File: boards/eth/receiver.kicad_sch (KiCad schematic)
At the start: 10 parts, among them U16 74HC74, U17 74HC04, U18 74HC161, U19 74HC4040, U20 74HC164, U7 74HC08

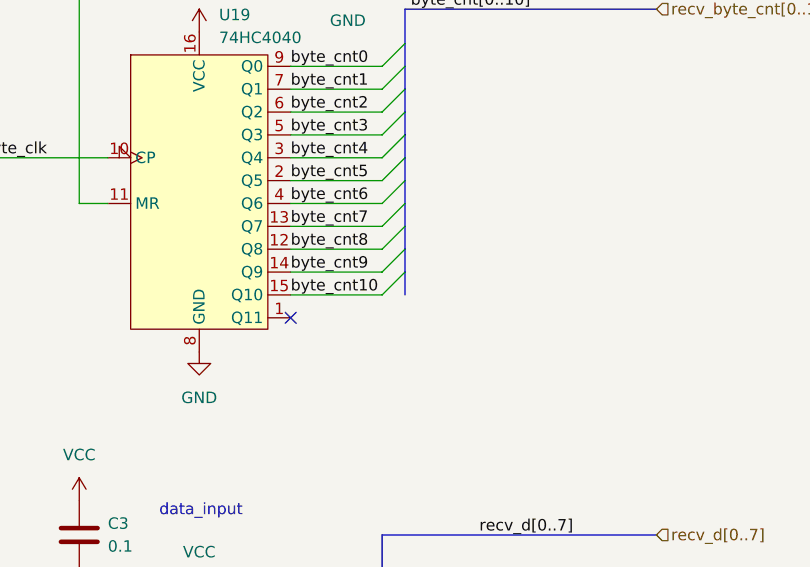
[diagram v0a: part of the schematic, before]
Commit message: Eth: transmitter schematics finished
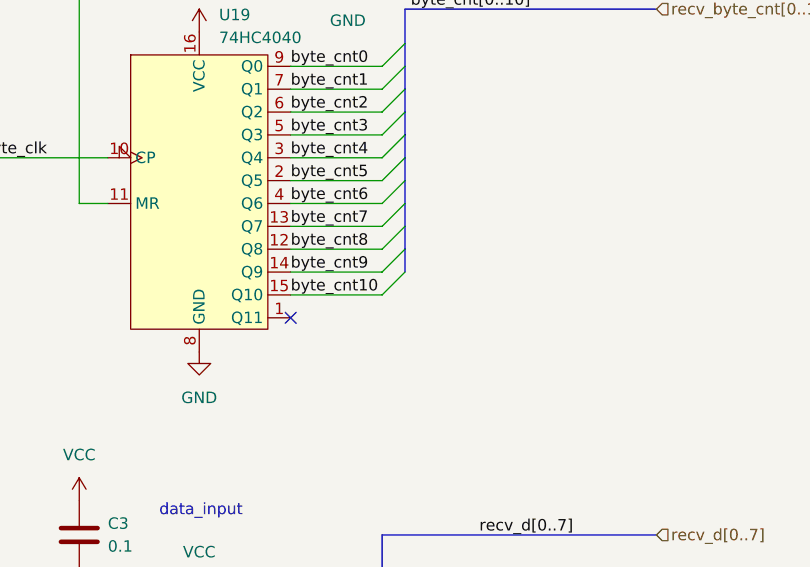
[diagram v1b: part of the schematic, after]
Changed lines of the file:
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@@
-    (stroke (width 0) (type default))
-  )
-  (bus (pts (xy 189.23 62.865) (xy 189.23 60.325))
     (stroke (width 0) (type default))
   )

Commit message: Eth: schematics checked
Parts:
- C30: renamed from C1; footprint (none) -> Capacitor_SMD:C_0805_2012Metric
- C31: renamed from C2; footprint (none) -> Capacitor_SMD:C_0805_2012Metric
- C32: renamed from C3; footprint (none) -> Capacitor_SMD:C_0805_2012Metric
- C33: renamed from C4; footprint (none) -> Capacitor_SMD:C_0805_2012Metric
- U29: renamed from U16; footprint (none) -> Package_SO:TSSOP-14_4.4x5mm_P0.65mm
- U30: renamed from U18; footprint (none) -> Package_SO:TSSOP-16_4.4x5mm_P0.65mm
- U31: renamed from U19; footprint (none) -> Package_SO:TSSOP-16_4.4x5mm_P0.65mm
- U32: renamed from U20; footprint (none) -> Package_SO:TSSOP-14_4.4x5mm_P0.65mm
- U6: renamed from U7; footprint (none) -> Package_SO:TSSOP-14_4.4x5mm_P0.65mm
- U9: renamed from U17; footprint (none) -> Package_SO:TSSOP-14_4.4x5mm_P0.65mm

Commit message: Eth: untangle schematic
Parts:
- removed U9: 74HC04, Package_SO:TSSOP-14_4.4x5mm_P0.65mm, symbol 74xx:74HC04
- added C39: 0.1, Capacitor_SMD:C_0805_2012Metric, symbol Device:C
- added U37: 74HC04, Package_SO:TSSOP-14_4.4x5mm_P0.65mm, symbol 74xx:74HC04
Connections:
- net GND: now also C39.2, U37.1, U37.7 (GND)
- net VCC: now also C39.1, U37.13, U37.14 (VCC)
- net bit_count2: now also U37.9
- net rst: now also U37.10
- net ~{bit_count_2}: now also U37.8
- net ~{rst}: now also U37.11
- new net: U37.2, U37.3
- no-connect marks 7 -> 9
